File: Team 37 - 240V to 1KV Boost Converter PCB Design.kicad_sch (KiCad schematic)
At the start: 0 parts

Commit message: Just getting started. Rn, its just a Battery connected to a resistor with a wire
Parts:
- added BT1: Battery_Cell, symbol Device:Battery_Cell
- added D1: LED, symbol Device:LED
- added R1: R_US, symbol Device:R_US
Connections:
- new net: BT1.1 (+), R1.1
- new net: D1.1 (K), R1.2
- new net: BT1.2 (-), D1.2 (A)

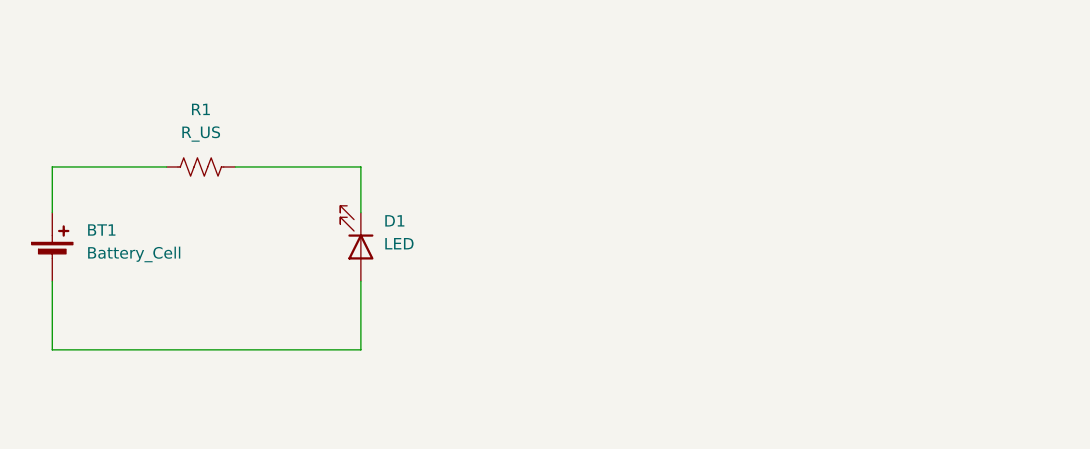
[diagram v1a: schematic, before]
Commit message: Circuit Schematic (Without Imported Models)
I made the circuit schematic in there. Need to:
*Import the model footprints
*Add snubber Resistor
*Add pull-down Resistor
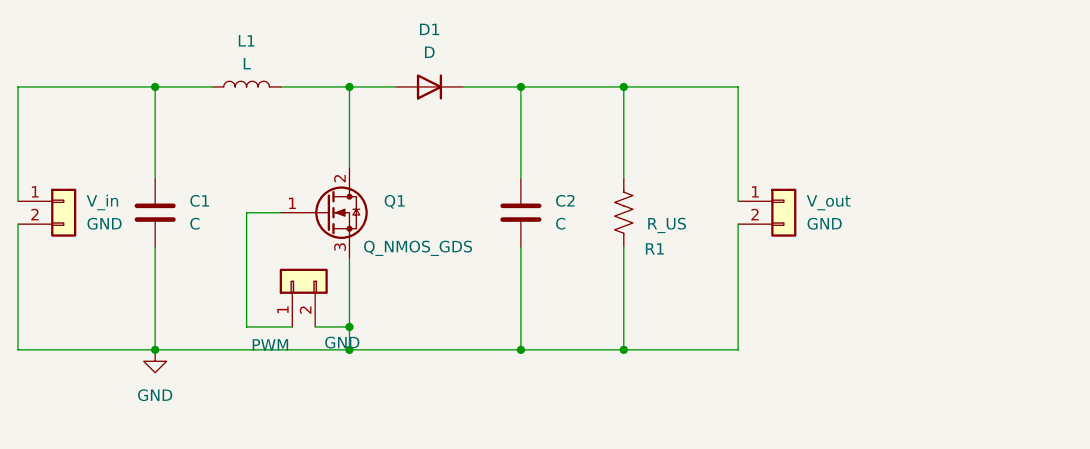
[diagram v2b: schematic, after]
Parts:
- removed BT1: Battery_Cell, symbol Device:Battery_Cell
- removed D1: LED, symbol Device:LED
- added C1, C2: C, symbol Device:C
- added D1: D, symbol Device:D
- added L1: L, symbol Device:L
- added PWM, V_in, V_out: GND, symbol Connector_Generic:Conn_01x02
- added Q1: Q_NMOS_GDS, symbol Transistor_FET:Q_NMOS_GDS
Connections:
- net at R1.1: now also C2.1, D1.1 (K), V_out.1 (Pin_1)
- net GND: now reaches R1.2
- net GND: now also C1.2, C2.2, PWM.2 (Pin_2), Q1.3 (S), V_in.2 (Pin_2), V_out.2 (Pin_2)
- new net: C1.1, L1.1, V_in.1 (Pin_1)
- new net: D1.2 (A), L1.2, Q1.2 (D)
- new net: PWM.1 (Pin_1), Q1.1 (G)

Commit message: IDK what i changed lol
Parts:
- added R2: R_US, symbol Device:R_US
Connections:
- net V_in: now reaches C1.1, L1.1, V_in.1 (Pin_1)
- net SW: now reaches D1.2 (A), L1.2, Q1.2 (D)
- net V_out: now reaches C2.1, D1.1 (K), R1.1, V_out.1 (Pin_1)
- net at Q1.1 (G): now also R2.1; no longer PWM.1 (Pin_1)
- new net PWM: PWM.1 (Pin_1), R2.2
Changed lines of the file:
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@@
+	(wire
+		(pts
+			(xy 139.7 76.2) (xy 139.7 73.66)
+		)
+		(stroke
+			(width 0)
+			(type default)
+		)
+	)
 	(wire
 		(pts
@@
 	(wire
 		(pts
-			(xy 139.7 86.36) (xy 139.7 73.66)
+			(xy 139.7 86.36) (xy 139.7 83.82)
 		)
 		(stroke
@@
 			(width 0)
 			(type default)
+		)
+	)
+	(label "V_out"
+		(at 170.18 59.69 0)
+		(effects
+			(font
+				(size 1.27 1.27)
+			)
+			(justify left bottom)
+		)
+	)
+	(label "V_out"
+		(at 181.61 59.69 0)
+		(effects
+			(font
+				(size 1.27 1.27)
+			)
+			(justify left bottom)
+		)
+	)
+	(label "V_in"
+		(at 129.54 59.69 0)
+		(effects
+			(font
+				(size 1.27 1.27)
+			)
+			(justify left bottom)
+		)
+	)
+	(label "PWM"
+		(at 139.7 86.36 0)
+		(effects
+			(font
+				(size 1.27 1.27)
+			)
+			(justify left bottom)
+		)
+	)
+	(label "SW"
+		(at 151.13 59.69 0)
+		(effects
+			(font
+				(size 1.27 1.27)
+			)
+			(justify left bottom)
 		)
 	)
@@
 		(dnp no)
 		(property "Reference" "PWM"
-			(at 140.208 88.392 90)
+			(at 143.51 78.74 90)
 			(effects
 				(font
@@
 		(dnp no)
 		(property "Reference" "R1"
-			(at 183.896 77.724 0)
+			(at 183.642 73.914 0)
 			(effects
 				(font
@@
 				)
 				(justify left)
+				(hide yes)
 			)
 		)
@@
 					(unit 1)
 				)
+			)
+		)
+	)
+	(symbol
+		(lib_id "Device:R_US")
+		(at 139.7 80.01 0)
+		(unit 1)
+		(exclude_from_sim no)
+		(in_bom yes)
+		(on_board yes)
+		(dnp no)
+		(property "Reference" "R2"
+			(at 135.636 80.518 0)
+			(effects
+				(font
+					(size 1.27 1.27)
+				)
+				(justify left)
+			)
+		)
+		(property "Value" "R_US"
+			(at 134.112 82.296 0)
+			(effects
+				(font
+					(size 1.27 1.27)
+				)
+				(justify left)
+				(hide yes)
+			)
+		)
+		(property "Footprint" ""
+			(at 140.716 80.264 90)
+			(effects
+				(font
+					(size 1.27 1.27)
+				)
+				(hide yes)
+			)
+		)
+		(property "Datasheet" "~"
+			(at 139.7 80.01 0)
+			(effects
+				(font
+					(size 1.27 1.27)
+				)
+				(hide yes)
+			)
+		)
+		(property "Description" "Resistor, US symbol"
+			(at 139.7 80.01 0)
+			(effects
+				(font
+					(size 1.27 1.27)
+				)
+				(hide yes)
+			)
+		)
+		(pin "2"
+		)
+		(pin "1"
+		)
+		(instances
+			(project ""
+				(path "/abcb5957-4d06-4db5-8498-af728ead1f6d"
+					(reference "R2")
+					(unit 1)
+				)

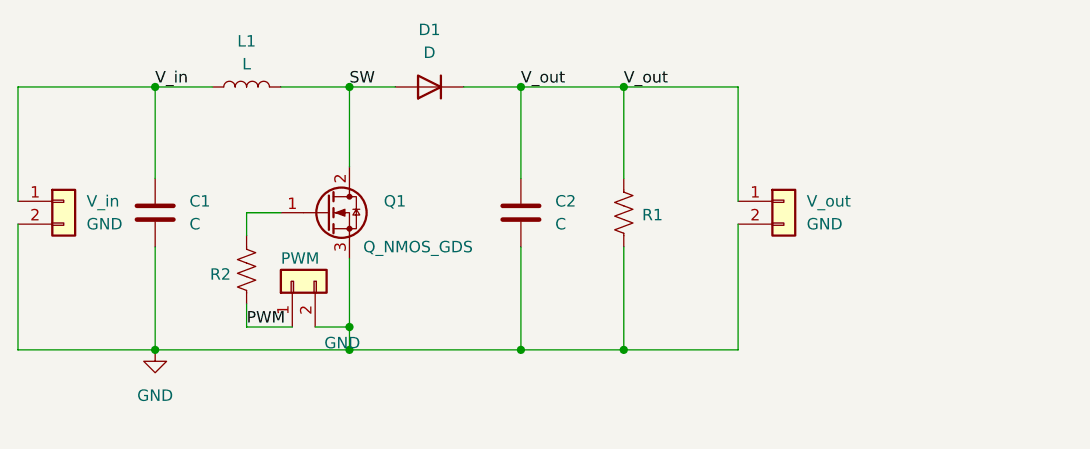
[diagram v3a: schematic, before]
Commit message: I added RC Snubber and Pull-down resistors.
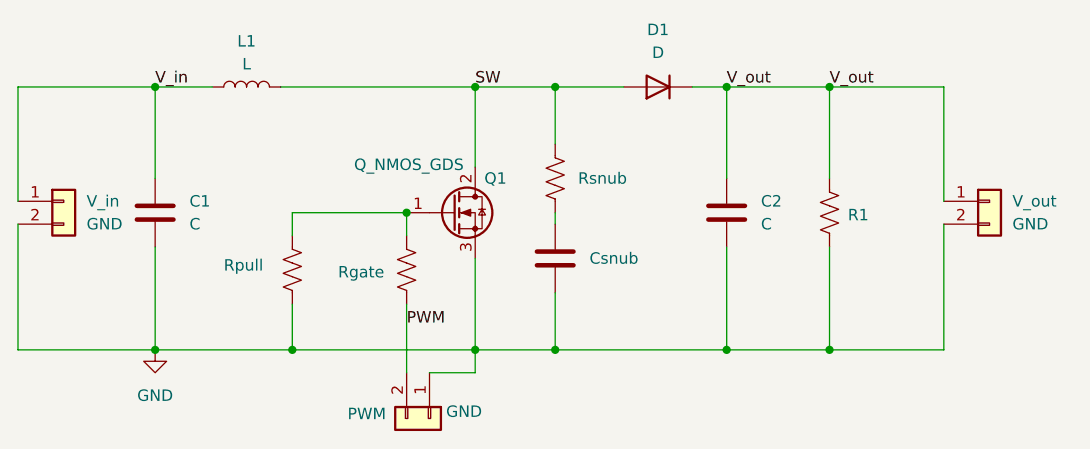
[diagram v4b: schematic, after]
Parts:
- added C3: Csnub, symbol Device:C
- added RC: Rsnub, symbol Device:R_US
- added Rpull: R_US, symbol Device:R_US
- renumbered R2 to Rgate
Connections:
- net GND: now also PWM.1 (Pin_1), C3.2, Rpull.2; no longer PWM.2 (Pin_2)
- net PWM: now also PWM.2 (Pin_2); no longer PWM.1 (Pin_1)
- net SW: now also RC.1
- net at Q1.1 (G), Rgate.1: now also Rpull.1
- new net: C3.1, RC.2
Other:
- moved on the sheet: C2, D1, PWM, Q1, R1, Rgate, V_out

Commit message: Still Struggling
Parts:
- removed Rgate, Rpull: R_US, symbol Device:R_US
- added R2: Rgate, symbol Device:R_US
- added R3: Rpull, symbol Device:R_US
- C2: value C -> Cout
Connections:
- net GND: now also R3.2
- net PWM: now also R2.2
- net at Q1.1 (G): now also R2.1, R3.1
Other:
- moved on the sheet: PWM

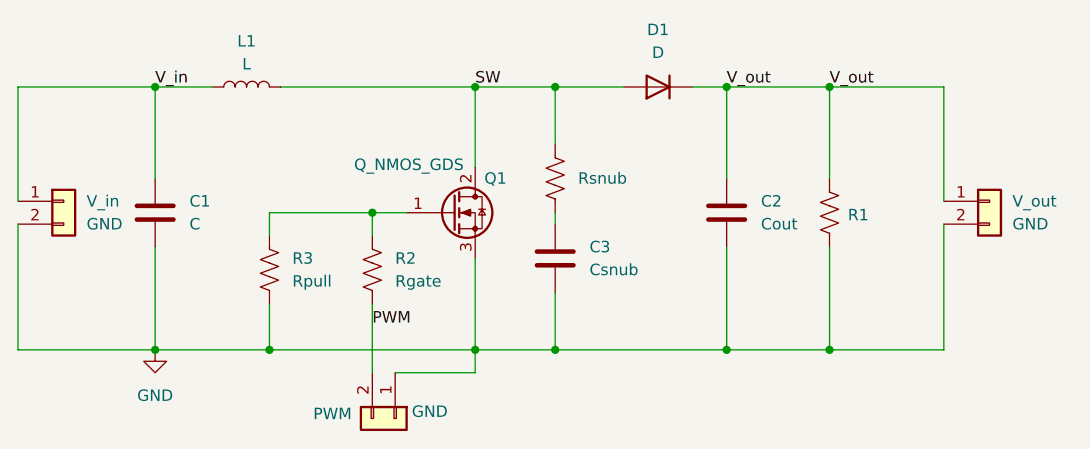
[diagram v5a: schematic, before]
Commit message: Added Infineon SiC Diode Model and Footprint
Imported Infineon IDWD10G200C5 SiC diode symbol and TO-247 footprint into project libraries and linked the schematic symbol to the footprint.
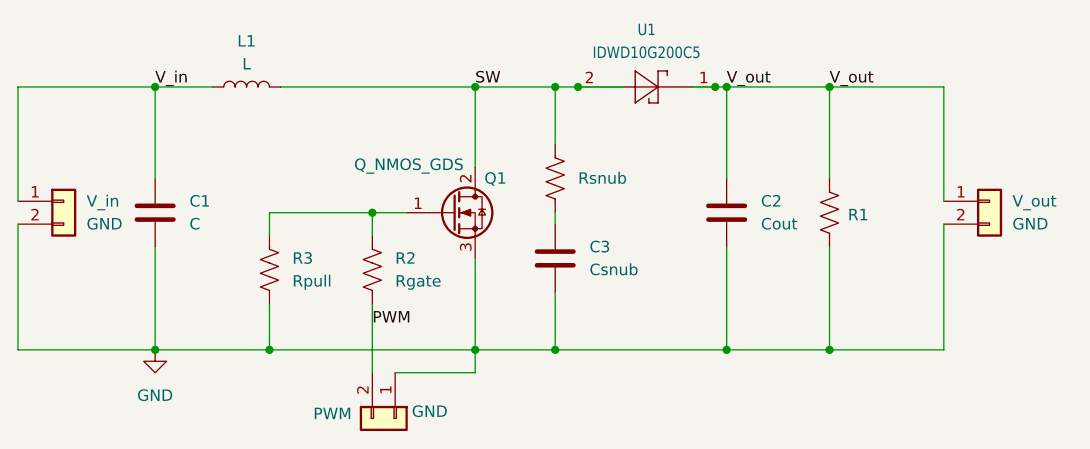
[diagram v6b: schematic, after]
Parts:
- removed D1: D, symbol Device:D
- added U1: IDWD10G200C5, project_footprints:IFX-PG-TO247-2-3, symbol project_symbols:IDWD10G200C5
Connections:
- net SW: now also U1.2 (ANODE)
- net V_out: now also U1.1 (CATHODE)
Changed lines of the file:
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@@
+	)
+	(junction
+		(at 191.77 59.69)
+		(diameter 0)
+		(color 0 0 0 0)
 	)
 	(junction
@@
 		(color 0 0 0 0)
 	)
+	(junction
+		(at 176.53 59.69)
+		(diameter 0)
+		(color 0 0 0 0)
+	)
 	(wire
 		(pts
@@
 	(wire
 		(pts
-			(xy 189.23 59.69) (xy 193.04 59.69)
+			(xy 189.23 59.69) (xy 191.77 59.69)
 		)
 		(stroke
@@
 	(wire
 		(pts
-			(xy 173.99 59.69) (xy 181.61 59.69)
+			(xy 173.99 59.69) (xy 176.53 59.69)
+		)
+		(stroke
+			(width 0)
+			(type default)
+		)
+	)
+	(wire
+		(pts
+			(xy 191.77 59.69) (xy 193.04 59.69)
 		)
 		(stroke
@@
 		(pts
 			(xy 143.51 59.69) (xy 165.1 59.69)
+		)
+		(stroke
+			(width 0)
+			(type default)
+		)
+	)
+	(wire
+		(pts
+			(xy 176.53 59.69) (xy 181.61 59.69)
 		)
 		(stroke
@@
 	)
 	(symbol
+		(lib_id "project_symbols:IDWD10G200C5")
+		(at 179.07 57.15 0)
+		(unit 1)
+		(exclude_from_sim no)
+		(in_bom yes)
+		(on_board yes)
+		(dnp no)
+		(fields_autoplaced yes)
+		(property "Reference" "U1"
+			(at 184.15 53.34 0)
+			(effects
+				(font
+					(size 1.27 1.0795)
+				)
+			)
+		)
+		(property "Value" "IDWD10G200C5"
+			(at 184.15 55.88 0)
+			(effects
+				(font
+					(size 1.27 1.0795)
+				)
+			)
+		)
+		(property "Footprint" "project_footprints:IFX-PG-TO247-2-3"
+			(at 179.07 57.15 0)
+			(effects
+				(font
+					(size 1.27 1.27)
+				)
+				(hide yes)
+			)
+		)
+		(property "Datasheet" ""
+			(at 179.07 57.15 0)
+			(effects
+				(font
+					(size 1.27 1.27)
+				)
+				(hide yes)
+			)
+		)
+		(property "Description" "Standard Schottky Diode Symbol, 1 Cathode, 2 Anode"
+			(at 180.34 54.356 0)
+			(effects
+				(font
+					(size 1.27 1.27)
+				)
+				(hide yes)
+			)
+		)
+		(pin "2"
+		)
+		(pin "1"
+		)
+		(instances
+			(project ""
+				(path "/abcb5957-4d06-4db5-8498-af728ead1f6d"
+					(reference "U1")
+					(unit 1)
+				)
+			)
+		)
+	)
+	(symbol
 		(lib_id "Device:C")
 		(at 173.99 78.74 0)
@@
 					(unit 1)
 				)
-			)
-		)
-	)
-	(symbol
-		(lib_id "Device:D")
-		(at 185.42 59.69 180)
-		(unit 1)
-		(exclude_from_sim no)
-		(in_bom yes)
-		(on_board yes)
-		(dnp no)
-		(fields_autoplaced yes)
-		(property "Reference" "D1"
-			(at 185.42 53.34 0)
-			(effects
-				(font
-					(size 1.27 1.27)
-				)
-			)
-		)
-		(property "Value" "D"
-			(at 185.42 55.88 0)
-			(effects
-				(font
-					(size 1.27 1.27)
-				)
-			)
-		)
-		(property "Footprint" ""
-			(at 185.42 59.69 0)
-			(effects
-				(font
-					(size 1.27 1.27)
-				)
-				(hide yes)
-			)
-		)
-		(property "Datasheet" "~"
-			(at 185.42 59.69 0)
-			(effects
-				(font
-					(size 1.27 1.27)
-				)
-				(hide yes)
-			)
-		)
-		(property "Description" "Diode"
-			(at 185.42 59.69 0)
-			(effects
-				(font
-					(size 1.27 1.27)
-				)
-				(hide yes)
-			)
-		)
-		(property "Sim.Device" "D"
-			(at 185.42 59.69 0)
-			(effects
-				(font
-					(size 1.27 1.27)
-				)
-				(hide yes)
-			)
-		)
-		(property "Sim.Pins" "1=K 2=A"
-			(at 185.42 59.69 0)
-			(effects
-				(font
-					(size 1.27 1.27)
-				)
-				(hide yes)
-			)
-		)
-		(pin "2"
-		)
-		(pin "1"
-		)
-		(instances
-			(project ""
-				(path "/abcb5957-4d06-4db5-8498-af728ead1f6d"
-					(reference "D1")
-					(unit 1)
-				)
